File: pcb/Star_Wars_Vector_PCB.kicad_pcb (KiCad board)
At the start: 2 copper layers, 292.1 x 524.5 mm, 352 parts, among them J17 Main_Connector, J20 Edge_Connector_30_Pin, Q1 2N3904, Q4 2N3904, Q5 2N3904, Q6 2N3904, Q7 2N3904, Q8 2N3906

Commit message: Updated PCB design and added BOM
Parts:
- moved J20 1.33 mm to (79.8, 55.2)
- moved REF** 0.63 mm to (69.8, 60.3)
- moved REF** 0.63 mm to (144.8, 60.3)
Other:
- board size 292.1 x 524.5 mm -> 292.1 x 525.8 mm
- board text added: "12MHZ"
- board text added: "Designed By Nick Mikstas"
- board text added: "K"
- board text added: "ZREF"
- board text removed: "-"

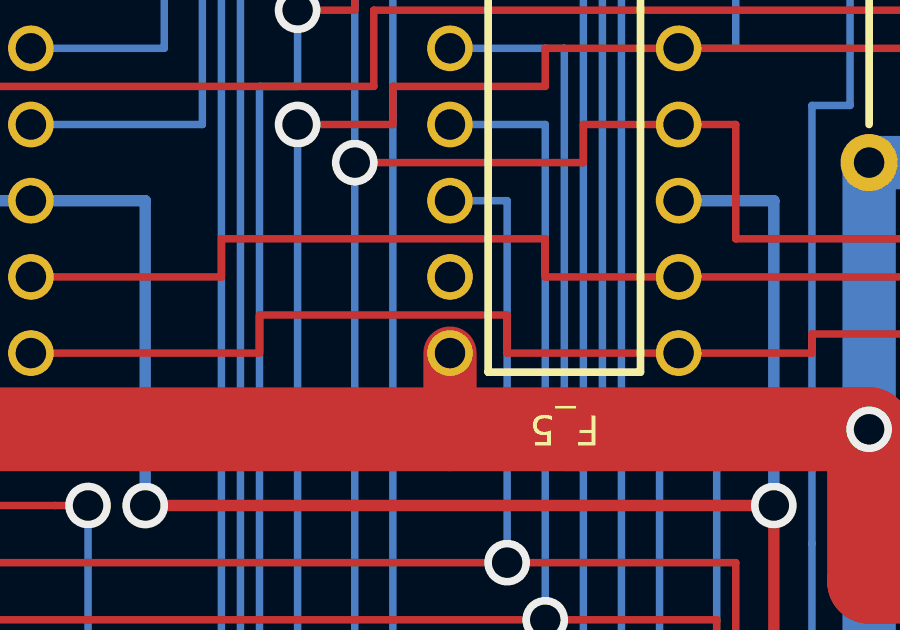
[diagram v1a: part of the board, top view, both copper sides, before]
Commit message: Fixed errors on the schematic
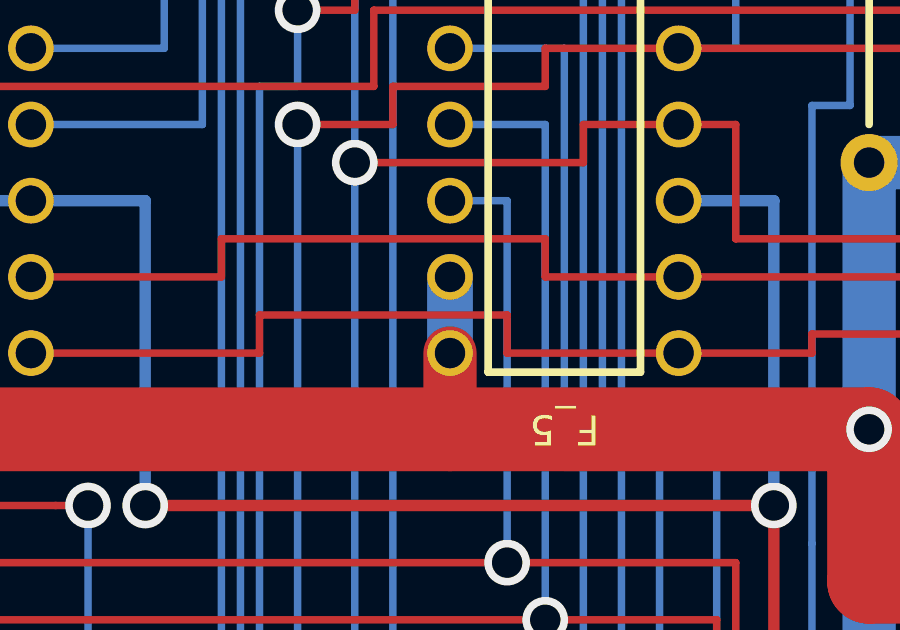
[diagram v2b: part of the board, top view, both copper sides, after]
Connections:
- F_5 pad 7: Net-(F_5-Pad7) -> GND
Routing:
- net GND: track 6402.1 -> 6404.6 mm
